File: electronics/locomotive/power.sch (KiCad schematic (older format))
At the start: 7 parts

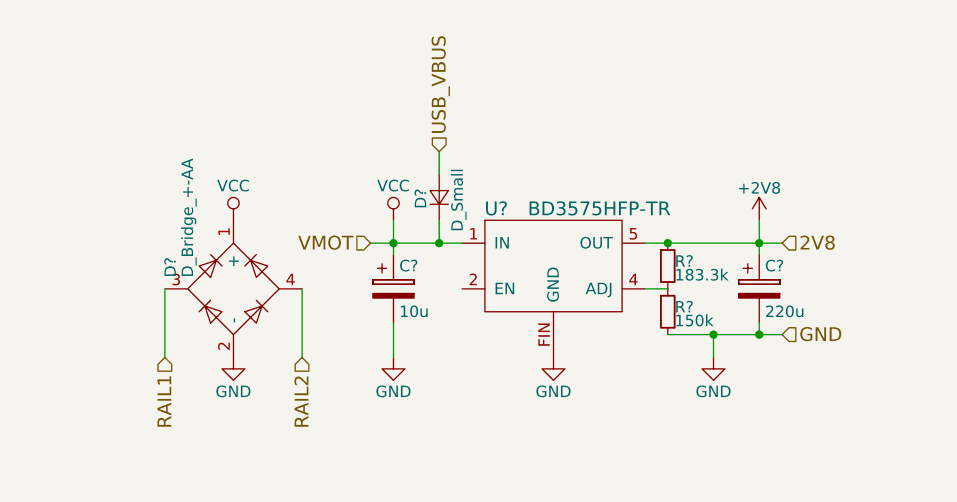
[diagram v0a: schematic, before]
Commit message: electronics: locomotive: Update schematics
Voltage regulator, TOF, IR receiver, voltage scaler, I2C control lines, power
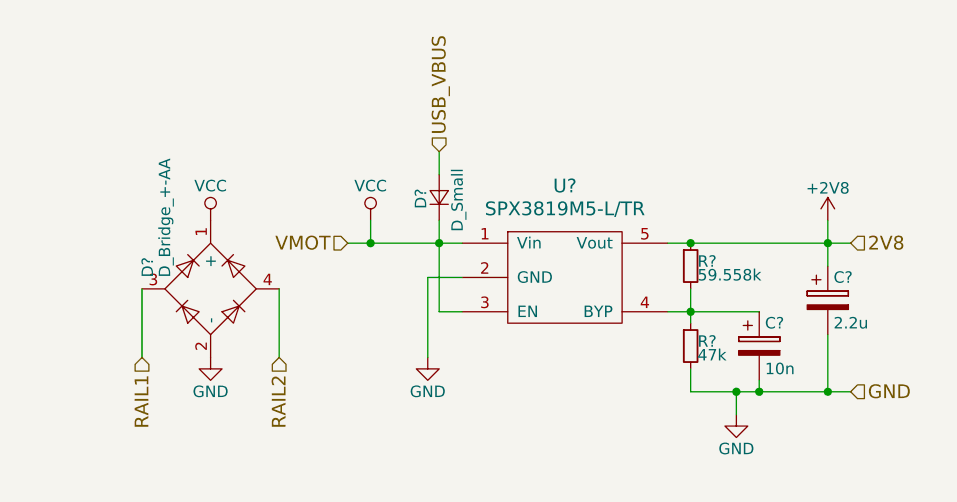
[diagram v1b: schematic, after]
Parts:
- removed C?: 220u, symbol CP
- removed C?: 10u, symbol CP
- removed U?: BD3575HFP-TR, symbol BD3575HFP-TR
- added C?: 2.2u, symbol CP
- added C?: 10n, symbol CP
- added U?: SPX3819M5-L/TR, symbol SPX3819M5-L/TR
- R?: value 183.3k -> 59.558k
- R?: value 150k -> 47k
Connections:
- net +2V8: now also C?.1, U?.5 (Vout)
- net GND: now also C?.2, C?.2, U?.2 (GND)
- net VCC: now also U?.1 (Vin), U?.3 (EN)
- net at R?.1, R?.2: now also C?.1, U?.4 (BYP)
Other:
- moved on the sheet: D?, R?
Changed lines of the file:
@@
 LIBS:valves
 LIBS:stm32
+LIBS:SPX3819
 LIBS:bcan
+LIBS:TSOP57238
 LIBS:locomotive-cache
 EELAYER 25 0
@@
 $EndDescr
 $Comp
-L BD3575HFP-TR U?
-U 1 1 58B1C552
-P 5800 3700
-F 0 "U?" H 5550 3950 60  0000 C CNN
-F 1 "BD3575HFP-TR" H 6000 3950 60  0000 C CNN
-F 2 "" H 5800 3700 60  0001 C CNN
-F 3 "" H 5800 3700 60  0001 C CNN
-	1    5800 3700
-	1    0    0    -1
-$EndComp
-$Comp
 L R_Small R?
 U 1 1 58B1C580
-P 6300 3700
-F 0 "R?" H 6330 3720 50  0000 L CNN
-F 1 "183.3k" H 6330 3660 50  0000 L CNN
-F 2 "" H 6300 3700 50  0001 C CNN
-F 3 "" H 6300 3700 50  0001 C CNN
-	1    6300 3700
+P 6400 3700
+F 0 "R?" H 6430 3720 50  0000 L CNN
+F 1 "59.558k" H 6430 3660 50  0000 L CNN
+F 2 "" H 6400 3700 50  0001 C CNN
+F 3 "" H 6400 3700 50  0001 C CNN
+	1    6400 3700
 	1    0    0    -1
 $EndComp
@@
 L R_Small R?
 U 1 1 58B1C5D4
-P 6300 3900
-F 0 "R?" H 6330 3920 50  0000 L CNN
-F 1 "150k" H 6330 3860 50  0000 L CNN
-F 2 "" H 6300 3900 50  0001 C CNN
-F 3 "" H 6300 3900 50  0001 C CNN
-	1    6300 3900
-	1    0    0    -1
-$EndComp
-Wire Wire Line
-	6200 3800 6300 3800
-Wire Wire Line
-	6200 3600 6800 3600
-Connection ~ 6300 3600
-Wire Wire Line
-	6300 4000 6800 4000
-Wire Wire Line
-	6500 4000 6500 4100
-Connection ~ 6500 4000
-$Comp
-L GND #PWR?
+P 6400 4050
+F 0 "R?" H 6430 4070 50  0000 L CNN
+F 1 "47k" H 6430 4010 50  0000 L CNN
+F 2 "" H 6400 4050 50  0001 C CNN
+F 3 "" H 6400 4050 50  0001 C CNN
+	1    6400 4050
+	1    0    0    -1
+$EndComp
+Wire Wire Line
+	6300 3600 7100 3600
+Connection ~ 6400 3600
+Wire Wire Line
+	6400 4250 7100 4250
+Wire Wire Line
+	6600 4250 6600 4350
+Connection ~ 6600 4250
+$Comp
+L GND #PWR031
 U 1 1 58B1C6C8
-P 5800 4100
-F 0 "#PWR?" H 5800 3850 50  0001 C CNN
-F 1 "GND" H 5800 3950 50  0000 C CNN
-F 2 "" H 5800 4100 50  0001 C CNN
-F 3 "" H 5800 4100 50  0001 C CNN
-	1    5800 4100
-	1    0    0    -1
-$EndComp
-$Comp
-L GND #PWR?
+P 5250 4100
+F 0 "#PWR031" H 5250 3850 50  0001 C CNN
+F 1 "GND" H 5250 3950 50  0000 C CNN
+F 2 "" H 5250 4100 50  0001 C CNN
+F 3 "" H 5250 4100 50  0001 C CNN
+	1    5250 4100
+	1    0    0    -1
+$EndComp
+$Comp
+L GND #PWR032
 U 1 1 58B1C6E4
-P 6500 4100
-F 0 "#PWR?" H 6500 3850 50  0001 C CNN
-F 1 "GND" H 6500 3950 50  0000 C CNN
-F 2 "" H 6500 4100 50  0001 C CNN
-F 3 "" H 6500 4100 50  0001 C CNN
-	1    6500 4100
-	1    0    0    -1
-$EndComp
-$Comp
-L CP C?
-U 1 1 58B1C779
-P 6700 3800
-F 0 "C?" H 6725 3900 50  0000 L CNN
-F 1 "220u" H 6725 3700 50  0000 L CNN
-F 2 "" H 6738 3650 50  0001 C CNN
-F 3 "" H 6700 3800 50  0001 C CNN
-	1    6700 3800
-	1    0    0    -1
-$EndComp
-Wire Wire Line
-	6700 3500 6700 3650
-Wire Wire Line
-	6700 4000 6700 3950
-$Comp
-L CP C?
-U 1 1 58B1C99F
-P 5100 3800
-F 0 "C?" H 5125 3900 50  0000 L CNN
-F 1 "10u" H 5125 3700 50  0000 L CNN
-F 2 "" H 5138 3650 50  0001 C CNN
-F 3 "" H 5100 3800 50  0001 C CNN
-	1    5100 3800
-	1    0    0    -1
-$EndComp
-$Comp
-L GND #PWR?
-U 1 1 58B1C9F6
-P 5100 4100
-F 0 "#PWR?" H 5100 3850 50  0001 C CNN
-F 1 "GND" H 5100 3950 50  0000 C CNN
-F 2 "" H 5100 4100 50  0001 C CNN
-F 3 "" H 5100 4100 50  0001 C CNN
-	1    5100 4100
-	1    0    0    -1
-$EndComp
-Wire Wire Line
-	5100 4100 5100 3950
-Wire Wire Line
-	5100 3500 5100 3650
-Connection ~ 5100 3600
-$Comp
-L +2V8 #PWR?
+P 6600 4350
+F 0 "#PWR032" H 6600 4100 50  0001 C CNN
+F 1 "GND" H 6600 4200 50  0000 C CNN
+F 2 "" H 6600 4350 50  0001 C CNN
+F 3 "" H 6600 4350 50  0001 C CNN
+	1    6600 4350
+	1    0    0    -1
+$EndComp
+Wire Wire Line
+	5000 3500 5000 3600
+Connection ~ 5000 3600
+$Comp
+L +2V8 #PWR033
 U 1 1 58B1CAFB
-P 6700 3500
-F 0 "#PWR?" H 6700 3350 50  0001 C CNN
-F 1 "+2V8" H 6700 3640 50  0000 C CNN
-F 2 "" H 6700 3500 50  0001 C CNN
-F 3 "" H 6700 3500 50  0001 C CNN
-	1    6700 3500
-	1    0    0    -1
-$EndComp
-Connection ~ 6700 3600
-$Comp
-L VCC #PWR?
+P 7000 3500
+F 0 "#PWR033" H 7000 3350 50  0001 C CNN
+F 1 "+2V8" H 7000 3640 50  0000 C CNN
+F 2 "" H 7000 3500 50  0001 C CNN
+F 3 "" H 7000 3500 50  0001 C CNN
+	1    7000 3500
+	1    0    0    -1
+$EndComp
+Connection ~ 7000 3600
+$Comp
+L VCC #PWR034
 U 1 1 58B1CB3C
-P 5100 3500
-F 0 "#PWR?" H 5100 3350 50  0001 C CNN
-F 1 "VCC" H 5100 3650 50  0000 C CNN
-F 2 "" H 5100 3500 50  0001 C CNN
-F 3 "" H 5100 3500 50  0001 C CNN
-	1    5100 3500
-	1    0    0    -1
-$EndComp
-Wire Wire Line
-	5000 3600 5400 3600
+P 5000 3500
+F 0 "#PWR034" H 5000 3350 50  0001 C CNN
+F 1 "VCC" H 5000 3650 50  0000 C CNN
+F 2 "" H 5000 3500 50  0001 C CNN
+F 3 "" H 5000 3500 50  0001 C CNN
+	1    5000 3500
+	1    0    0    -1
+$EndComp
+Wire Wire Line
+	4900 3600 5400 3600
 $Comp
 L D_Bridge_+-AA D?
 U 1 1 58B1CD4E
-P 4400 3800
-F 0 "D?" H 4450 4075 50  0000 L CNN
-F 1 "D_Bridge_+-AA" H 4450 4000 50  0000 L CNN
-F 2 "" H 4400 3800 50  0001 C CNN
-F 3 "" H 4400 3800 50  0001 C CNN
-	1    4400 3800
+P 4300 3800
+F 0 "D?" H 4350 4075 50  0000 L CNN
+F 1 "D_Bridge_+-AA" H 4350 4000 50  0000 L CNN
+F 2 "" H 4300 3800 50  0001 C CNN
+F 3 "" H 4300 3800 50  0001 C CNN
+	1    4300 3800
 	0    -1   -1   0
 $EndComp
 Wire Wire Line
-	4100 3800 4100 4100
-Wire Wire Line
-	4700 3800 4700 4100
-$Comp
-L GND #PWR?
+	4000 3800 4000 4100
+Wire Wire Line
+	4600 3800 4600 4100
+$Comp
+L GND #PWR035
 U 1 1 58B1D03D
-P 4400 4100
-F 0 "#PWR?" H 4400 3850 50  0001 C CNN
-F 1 "GND" H 4400 3950 50  0000 C CNN
-F 2 "" H 4400 4100 50  0001 C CNN
-F 3 "" H 4400 4100 50  0001 C CNN
-	1    4400 4100
-	1    0    0    -1
-$EndComp
-$Comp
-L VCC #PWR?
+P 4300 4100
+F 0 "#PWR035" H 4300 3850 50  0001 C CNN
+F 1 "GND" H 4300 3950 50  0000 C CNN
+F 2 "" H 4300 4100 50  0001 C CNN
+F 3 "" H 4300 4100 50  0001 C CNN
+	1    4300 4100
+	1    0    0    -1
+$EndComp
+$Comp
+L VCC #PWR036
 U 1 1 58B1D05A
-P 4400 3500
-F 0 "#PWR?" H 4400 3350 50  0001 C CNN
-F 1 "VCC" H 4400 3650 50  0000 C CNN
-F 2 "" H 4400 3500 50  0001 C CNN
-F 3 "" H 4400 3500 50  0001 C CNN
-	1    4400 3500
-	1    0    0    -1
-$EndComp
-Text HLabel 4100 4100 3    60   Input ~ 0
+P 4300 3500
+F 0 "#PWR036" H 4300 3350 50  0001 C CNN
+F 1 "VCC" H 4300 3650 50  0000 C CNN
+F 2 "" H 4300 3500 50  0001 C CNN
+F 3 "" H 4300 3500 50  0001 C CNN
+	1    4300 3500
+	1    0    0    -1
+$EndComp
+Text HLabel 4000 4100 3    60   Input ~ 0
 RAIL1
-Text HLabel 4700 4100 3    60   Input ~ 0
+Text HLabel 4600 4100 3    60   Input ~ 0
 RAIL2
-Text HLabel 6800 3600 2    60   Input ~ 0
+Text HLabel 7100 3600 2    60   Input ~ 0
 2V8
-Connection ~ 6700 4000
-Text HLabel 6800 4000 2    60   Input ~ 0
+Connection ~ 7000 4250
+Text HLabel 7100 4250 2    60   Input ~ 0
 GND
-Text HLabel 5000 3600 0    60   Input ~ 0
+Text HLabel 4900 3600 0    60   Input ~ 0
 VMOT
 $Comp
@@
 $EndComp
 Wire Wire Line
-	5300 3600 5300 3500
+	5300 3500 5300 3900
 Connection ~ 5300 3600
 Wire Wire Line
@@
 Text HLabel 5300 3200 1    60   Input ~ 0
 USB_VBUS
+Wire Wire Line
+	6400 3800 6400 3950
+Wire Wire Line
+	6300 3900 6700 3900
+Connection ~ 6400 3900
+Wire Wire Line
+	7000 3500 7000 3700
+Wire Wire Line
+	5250 3750 5400 3750
+Wire Wire Line
+	5250 3750 5250 4100
+Wire Wire Line
+	5300 3900 5400 3900
+$Comp
+L CP C?
+U 1 1 58C52450
+P 7000 3850
+F 0 "C?" H 7025 3950 50  0000 L CNN
+F 1 "2.2u" H 7025 3750 50  0000 L CNN
+F 2 "" H 7038 3700 50  0001 C CNN
+F 3 "" H 7000 3850 50  0001 C CNN
+	1    7000 3850
+	1    0    0    -1
+$EndComp
+Wire Wire Line
+	7000 4000 7000 4250
+$Comp
+L CP C?
+U 1 1 58C525A9
+P 6700 4050
+F 0 "C?" H 6725 4150 50  0000 L CNN
+F 1 "10n" H 6725 3950 50  0000 L CNN
+F 2 "" H 6738 3900 50  0001 C CNN
+F 3 "" H 6700 4050 50  0001 C CNN
+	1    6700 4050
+	1    0    0    -1
+$EndComp
+Wire Wire Line
+	6400 4150 6400 4250
+Wire Wire Line
+	6700 4200 6700 4250
+Connection ~ 6700 4250
+$Comp
+L SPX3819M5-L/TR U?
+U 1 1 58C52EC6
+P 5850 3450
+F 0 "U?" H 5850 3550 60  0000 C CNN
+F 1 "SPX3819M5-L/TR" H 5850 3450 60  0000 C CNN
+F 2 "" H 5850 3400 60  0001 C CNN
+F 3 "" H 5850 3400 60  0001 C CNN
+	1    5850 3450
+	1    0    0    -1
+$EndComp
 $EndSCHEMATC

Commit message: firmware: locomotive: Change voltage regulator resistor values
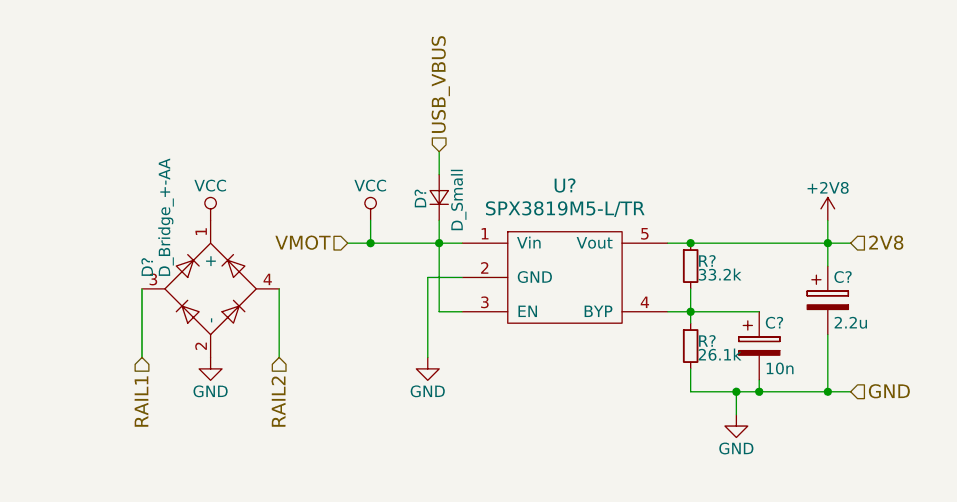
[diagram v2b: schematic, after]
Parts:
- R?: value 59.558k -> 33.2k
- R?: value 47k -> 26.1k
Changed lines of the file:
@@
 P 6400 3700
 F 0 "R?" H 6430 3720 50  0000 L CNN
-F 1 "59.558k" H 6430 3660 50  0000 L CNN
+F 1 "33.2k" H 6430 3660 50  0000 L CNN
 F 2 "" H 6400 3700 50  0001 C CNN
 F 3 "" H 6400 3700 50  0001 C CNN
@@
 P 6400 4050
 F 0 "R?" H 6430 4070 50  0000 L CNN
-F 1 "47k" H 6430 4010 50  0000 L CNN
+F 1 "26.1k" H 6430 4010 50  0000 L CNN
 F 2 "" H 6400 4050 50  0001 C CNN
 F 3 "" H 6400 4050 50  0001 C CNN

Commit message: electronics: locomotive: Fix up schematics
- add all parts and label them
- some values still tentative
- still need to finish connectors
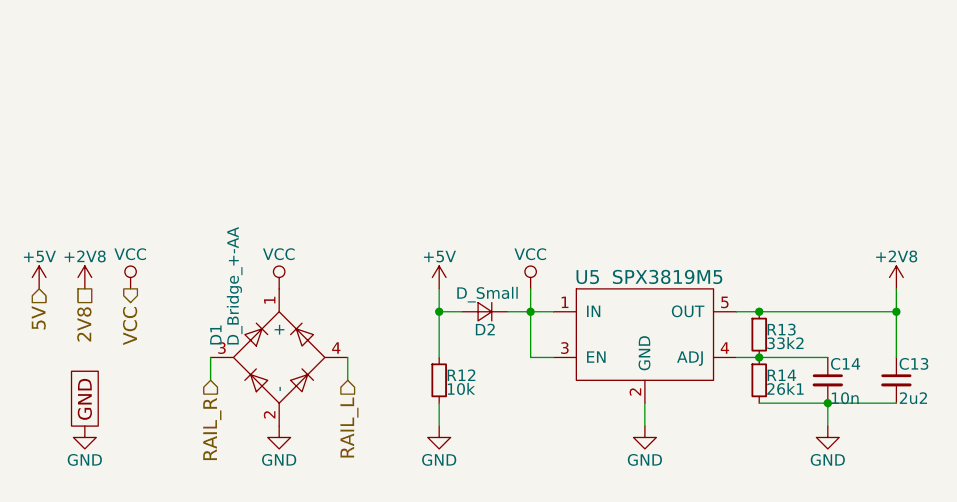
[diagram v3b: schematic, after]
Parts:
- removed C?: 2.2u, symbol CP
- removed C?: 10n, symbol CP
- removed U?: SPX3819M5-L/TR, symbol SPX3819M5-L/TR
- added C13: 2u2, symbol C_Small
- added C14: 10n, symbol C_Small
- added R12: 10k, symbol R_Small
- added U5: SPX3819M5, symbol SPX3819M5
- R13: renamed from R?; value 33.2k -> 33k2
- R14: renamed from R?; value 26.1k -> 26k1
- gave numbers to parts that had none: 2
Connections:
- net +2V8: now also C13.1, U5.5 (OUT)
- net GND: now also C13.2, C14.2, R12.2, U5.2 (GND)
- net VCC: now also U5.1 (IN), U5.3 (EN)
- net at R13.2, R14.1: now also C14.1, U5.4 (ADJ)
- net RAIL1 renamed RAIL_R
- net RAIL2 renamed RAIL_L
- net USB_VBUS renamed +5V
- net +5V: now also R12.1
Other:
- moved on the sheet: D1, D2, R13, R14

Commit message: electronics: locomotive: Board Rev 1.0
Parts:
- C13, C14: footprint (none) -> Capacitors_SMD:C_0603
- D1: value D_Bridge_+-AA -> CDBHM240L-HF; footprint (none) -> bcan:TO-269AA
- D2: value D_Small -> CUS08F30; footprint (none) -> Diodes_SMD:D_SOD-323
- R12, R13, R14: footprint (none) -> Resistors_SMD:R_0603
- U5: footprint (none) -> TO_SOT_Packages_SMD:SOT-23-5
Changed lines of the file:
@@
 F 0 "R13" H 6730 4020 50  0000 L CNN
 F 1 "33k2" H 6730 3960 50  0000 L CNN
-F 2 "" H 6700 4000 50  0001 C CNN
+F 2 "Resistors_SMD:R_0603" H 6700 4000 50  0001 C CNN
 F 3 "" H 6700 4000 50  0001 C CNN
 	1    6700 4000
@@
 F 0 "R14" H 6730 4220 50  0000 L CNN
 F 1 "26k1" H 6730 4160 50  0000 L CNN
-F 2 "" H 6700 4200 50  0001 C CNN
+F 2 "Resistors_SMD:R_0603" H 6700 4200 50  0001 C CNN
 F 3 "" H 6700 4200 50  0001 C CNN
 	1    6700 4200
@@
 $EndComp
 $Comp
-L GND #PWR054
+L GND #PWR035
 U 1 1 58B1C6C8
 P 6200 4400
-F 0 "#PWR054" H 6200 4150 50  0001 C CNN
+F 0 "#PWR035" H 6200 4150 50  0001 C CNN
 F 1 "GND" H 6200 4250 50  0000 C CNN
 F 2 "" H 6200 4400 50  0001 C CNN
@@
 $EndComp
 $Comp
-L GND #PWR055
+L GND #PWR036
 U 1 1 58B1C6E4
 P 7000 4400
-F 0 "#PWR055" H 7000 4150 50  0001 C CNN
+F 0 "#PWR036" H 7000 4150 50  0001 C CNN
 F 1 "GND" H 7000 4250 50  0000 C CNN
 F 2 "" H 7000 4400 50  0001 C CNN
@@
 $EndComp
 $Comp
-L +2V8 #PWR056
+L +2V8 #PWR037
 U 1 1 58B1CAFB
 P 7300 3800
-F 0 "#PWR056" H 7300 3650 50  0001 C CNN
+F 0 "#PWR037" H 7300 3650 50  0001 C CNN
 F 1 "+2V8" H 7300 3940 50  0000 C CNN
 F 2 "" H 7300 3800 50  0001 C CNN
@@
 $EndComp
 $Comp
-L VCC #PWR057
+L VCC #PWR038
 U 1 1 58B1CB3C
 P 5700 3800
-F 0 "#PWR057" H 5700 3650 50  0001 C CNN
+F 0 "#PWR038" H 5700 3650 50  0001 C CNN
 F 1 "VCC" H 5700 3950 50  0000 C CNN
 F 2 "" H 5700 3800 50  0001 C CNN
@@
 P 4600 4100
 F 0 "D1" H 4650 4375 50  0000 L CNN
-F 1 "D_Bridge_+-AA" H 4650 4300 50  0000 L CNN
-F 2 "" H 4600 4100 50  0001 C CNN
+F 1 "CDBHM240L-HF" H 4650 4300 50  0000 L CNN
+F 2 "bcan:TO-269AA" H 4600 4100 50  0001 C CNN
 F 3 "" H 4600 4100 50  0001 C CNN
 	1    4600 4100
@@
 $EndComp
 $Comp
-L GND #PWR058
+L GND #PWR039
 U 1 1 58B1D03D
 P 4600 4400
-F 0 "#PWR058" H 4600 4150 50  0001 C CNN
+F 0 "#PWR039" H 4600 4150 50  0001 C CNN
 F 1 "GND" H 4600 4250 50  0000 C CNN
 F 2 "" H 4600 4400 50  0001 C CNN
@@
 $EndComp
 $Comp
-L VCC #PWR059
+L VCC #PWR040
 U 1 1 58B1D05A
 P 4600 3800
-F 0 "#PWR059" H 4600 3650 50  0001 C CNN
+F 0 "#PWR040" H 4600 3650 50  0001 C CNN
 F 1 "VCC" H 4600 3950 50  0000 C CNN
 F 2 "" H 4600 3800 50  0001 C CNN
@@
 P 5500 3900
 F 0 "D2" H 5450 3980 50  0000 L CNN
-F 1 "D_Small" H 5350 3820 50  0000 L CNN
-F 2 "" V 5500 3900 50  0001 C CNN
+F 1 "CUS08F30" H 5350 3820 50  0000 L CNN
+F 2 "Diodes_SMD:D_SOD-323" V 5500 3900 50  0001 C CNN
 F 3 "" V 5500 3900 50  0001 C CNN
 	1    5500 3900
@@
 5V
 $Comp
-L +5V #PWR060
+L +5V #PWR041
 U 1 1 58D2A4F8
 P 5300 3800
-F 0 "#PWR060" H 5300 3650 50  0001 C CNN
+F 0 "#PWR041" H 5300 3650 50  0001 C CNN
 F 1 "+5V" H 5300 3940 50  0000 C CNN
 F 2 "" H 5300 3800 50  0001 C CNN
@@
 $EndComp
 $Comp
-L +2V8 #PWR061
+L +2V8 #PWR042
 U 1 1 58D2A53C
 P 3750 3800
-F 0 "#PWR061" H 3750 3650 50  0001 C CNN
+F 0 "#PWR042" H 3750 3650 50  0001 C CNN
 F 1 "+2V8" H 3750 3940 50  0000 C CNN
 F 2 "" H 3750 3800 50  0001 C CNN
@@
 $EndComp
 $Comp
-L GND #PWR062
+L GND #PWR043
 U 1 1 58D2A542
 P 3750 4400
-F 0 "#PWR062" H 3750 4150 50  0001 C CNN
+F 0 "#PWR043" H 3750 4150 50  0001 C CNN
 F 1 "GND" H 3750 4250 50  0000 C CNN
 F 2 "" H 3750 4400 50  0001 C CNN
@@
 2V8
 $Comp
-L +5V #PWR063
+L +5V #PWR044
 U 1 1 58D2A592
 P 3550 3800
-F 0 "#PWR063" H 3550 3650 50  0001 C CNN
+F 0 "#PWR044" H 3550 3650 50  0001 C CNN
 F 1 "+5V" H 3550 3940 50  0000 C CNN
 F 2 "" H 3550 3800 50  0001 C CNN
@@
 $EndComp
 $Comp
-L VCC #PWR064
+L VCC #PWR045
 U 1 1 58D2A5DE
 P 3950 3800
-F 0 "#PWR064" H 3950 3650 50  0001 C CNN
+F 0 "#PWR045" H 3950 3650 50  0001 C CNN
 F 1 "VCC" H 3950 3950 50  0000 C CNN
 F 2 "" H 3950 3800 50  0001 C CNN
@@
 F 0 "U5" H 5950 4250 60  0000 C CNN
 F 1 "SPX3819M5" H 6300 4250 60  0000 C CNN
-F 2 "" H 6200 4250 60  0001 C CNN
+F 2 "TO_SOT_Packages_SMD:SOT-23-5" H 6200 4250 60  0001 C CNN
 F 3 "" H 6200 4250 60  0001 C CNN
 	1    6200 4000
@@
 F 0 "C14" H 7010 4270 50  0000 L CNN
 F 1 "10n" H 7010 4120 50  0000 L CNN
-F 2 "" H 7000 4200 50  0001 C CNN
+F 2 "Capacitors_SMD:C_0603" H 7000 4200 50  0001 C CNN
 F 3 "" H 7000 4200 50  0001 C CNN
 	1    7000 4200
@@
 F 0 "C13" H 7310 4270 50  0000 L CNN
 F 1 "2u2" H 7310 4120 50  0000 L CNN
-F 2 "" H 7300 4200 50  0001 C CNN
+F 2 "Capacitors_SMD:C_0603" H 7300 4200 50  0001 C CNN
 F 3 "" H 7300 4200 50  0001 C CNN
 	1    7300 4200
@@
 F 0 "R12" H 5330 4220 50  0000 L CNN
 F 1 "10k" H 5330 4160 50  0000 L CNN
-F 2 "" H 5300 4200 50  0001 C CNN
+F 2 "Resistors_SMD:R_0603" H 5300 4200 50  0001 C CNN
 F 3 "" H 5300 4200 50  0001 C CNN
 	1    5300 4200
@@
 $EndComp
 $Comp
-L GND #PWR065
+L GND #PWR046
 U 1 1 58D38F8B
 P 5300 4400
-F 0 "#PWR065" H 5300 4150 50  0001 C CNN
+F 0 "#PWR046" H 5300 4150 50  0001 C CNN
 F 1 "GND" H 5300 4250 50  0000 C CNN
 F 2 "" H 5300 4400 50  0001 C CNN
